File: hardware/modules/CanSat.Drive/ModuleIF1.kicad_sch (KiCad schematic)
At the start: 12 parts, among them J5 Jumper, J6 Conn_01x04_MountingPin, U11 TCK106AF, U12 INA226

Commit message: シート追加
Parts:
- removed J5: Jumper, Connector_PinHeader_1.27mm:PinHeader_1x02_P1.27mm_Vertical, symbol Connector:Conn_01x02_Pin
- removed R23: 10k, Resistor_SMD:R_0402_1005Metric, symbol Device:R
- removed R26: 120, Resistor_SMD:R_0402_1005Metric, symbol Device:R
- removed U11: TCK106AF, WOBCLibrary:WCSPD-4(0.8x0.8), symbol WOBCLibrary:TCK106AF
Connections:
- net VIN renamed VOUT
- no-connect marks 0 -> 1

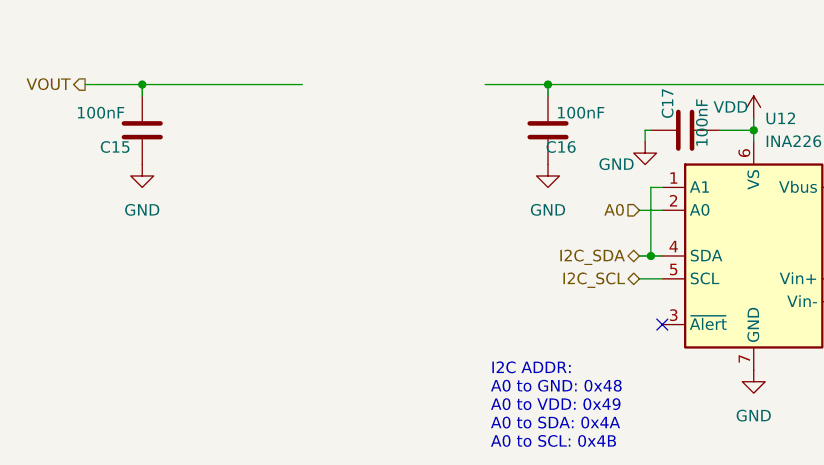
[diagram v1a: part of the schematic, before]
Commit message: 基板のフットプリントを作ったら回路図終わり
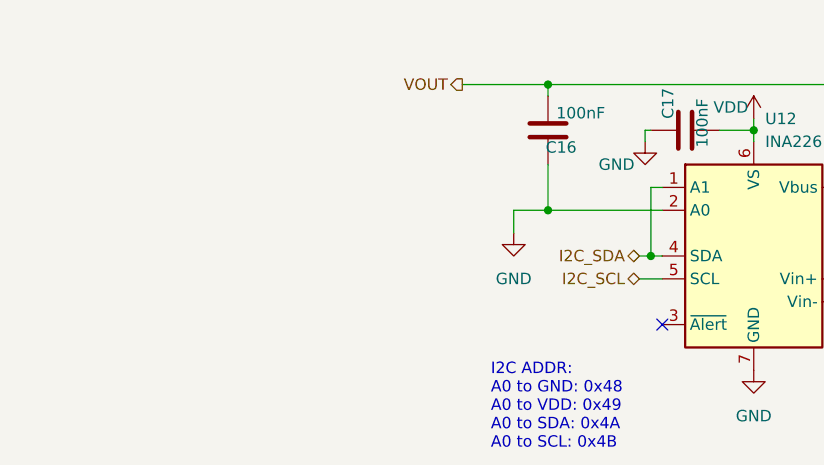
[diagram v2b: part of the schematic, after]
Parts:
- removed C15: 100nF, Capacitor_SMD:C_0402_1005Metric, symbol Device:C
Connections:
- net A0 is gone; now on net GND: U12.2 (A0)
- net VOUT: now also C16.2, R24.1, U12.10 (Vin+), U12.8 (Vbus)
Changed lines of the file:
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@@
 	)
 	(junction
-		(at 50.8 68.58)
+		(at 95.885 82.55)
 		(diameter 0)
 		(color 0 0 0 0)
@@
 	(wire
 		(pts
-			(xy 106.045 82.55) (xy 108.585 82.55)
+			(xy 95.885 82.55) (xy 108.585 82.55)
 		)
 		(stroke
@@
 	(wire
 		(pts
+			(xy 92.075 82.55) (xy 95.885 82.55)
+		)
+		(stroke
+			(width 0)
+			(type default)
+		)
+	)
+	(wire
+		(pts
 			(xy 107.315 80.01) (xy 107.315 87.63)
 		)
@@
 	(wire
 		(pts
-			(xy 44.45 68.58) (xy 50.8 68.58)
-		)
-		(stroke
-			(width 0)
-			(type default)
-		)
-	)
-	(wire
-		(pts
 			(xy 151.13 68.58) (xy 151.13 71.755)
 		)
@@
 	(wire
 		(pts
+			(xy 95.885 82.55) (xy 95.885 77.47)
+		)
+		(stroke
+			(width 0)
+			(type default)
+		)
+	)
+	(wire
+		(pts
 			(xy 106.045 87.63) (xy 107.315 87.63)
 		)
@@
 	(wire
 		(pts
-			(xy 50.8 68.58) (xy 50.8 69.85)
-		)
-		(stroke
-			(width 0)
-			(type default)
-		)
-	)
-	(wire
-		(pts
 			(xy 95.885 68.58) (xy 130.81 68.58)
 		)
@@
 	(wire
 		(pts
-			(xy 50.8 68.58) (xy 68.58 68.58)
+			(xy 86.36 68.58) (xy 95.885 68.58)
 		)
 		(stroke
@@
 	(wire
 		(pts
-			(xy 88.9 68.58) (xy 95.885 68.58)
-		)
-		(stroke
-			(width 0)
-			(type default)
-		)
-	)
-	(wire
-		(pts
 			(xy 130.81 68.58) (xy 130.81 80.01)
 		)
@@
 		(pts
 			(xy 118.745 73.66) (xy 118.745 74.93)
+		)
+		(stroke
+			(width 0)
+			(type default)
+		)
+	)
+	(wire
+		(pts
+			(xy 92.075 82.55) (xy 92.075 85.09)
 		)
 		(stroke
@@
 		)
 	)
-	(hierarchical_label "A0"
-		(shape input)
-		(at 106.045 82.55 180)
-		(fields_autoplaced yes)
-		(effects
-			(font
-				(size 1.27 1.27)
-			)
-			(justify right)
-		)
-	)
 	(hierarchical_label "I2C_SCL"
 		(shape bidirectional)
@@
 	(hierarchical_label "VOUT"
 		(shape output)
-		(at 44.45 68.58 180)
+		(at 86.36 68.58 180)
 		(fields_autoplaced yes)
 		(effects
@@
 			(project "GS"
 				(path "/953562b0-9f42-4c3d-8516-f6de553e7f3f/7e3ff05b-2209-4e68-8cf1-b7b284998fcd"
-					(reference "LED6")
+					(reference "LED301")
 					(unit 1)
 				)
@@
 			(project "GS"
 				(path "/953562b0-9f42-4c3d-8516-f6de553e7f3f/7e3ff05b-2209-4e68-8cf1-b7b284998fcd"
-					(reference "J6")
+					(reference "J301")
 					(unit 1)
 				)
@@
 			(project "GS"
 				(path "/953562b0-9f42-4c3d-8516-f6de553e7f3f/7e3ff05b-2209-4e68-8cf1-b7b284998fcd"
-					(reference "#PWR060")
+					(reference "#PWR0306")
 					(unit 1)
 				)
@@
 			(project "GS"
 				(path "/953562b0-9f42-4c3d-8516-f6de553e7f3f/7e3ff05b-2209-4e68-8cf1-b7b284998fcd"
-					(reference "U12")
+					(reference "U301")
 					(unit 1)
 				)
@@
 			(project "GS"
 				(path "/953562b0-9f42-4c3d-8516-f6de553e7f3f/7e3ff05b-2209-4e68-8cf1-b7b284998fcd"
-					(reference "#PWR059")
+					(reference "#PWR0305")
 					(unit 1)
 				)
@@
 			(project "GS"
 				(path "/953562b0-9f42-4c3d-8516-f6de553e7f3f/7e3ff05b-2209-4e68-8cf1-b7b284998fcd"
-					(reference "R25")
+					(reference "R302")
 					(unit 1)
 				)
@@
 			(project "GS"
 				(path "/953562b0-9f42-4c3d-8516-f6de553e7f3f/7e3ff05b-2209-4e68-8cf1-b7b284998fcd"
-					(reference "C17")
+					(reference "C302")
 					(unit 1)
 				)
@@
 			(project "GS"
 				(path "/953562b0-9f42-4c3d-8516-f6de553e7f3f/7e3ff05b-2209-4e68-8cf1-b7b284998fcd"
-					(reference "#PWR056")
+					(reference "#PWR0302")
 					(unit 1)
 				)
@@
 			(project "GS"
 				(path "/953562b0-9f42-4c3d-8516-f6de553e7f3f/7e3ff05b-2209-4e68-8cf1-b7b284998fcd"
-					(reference "#PWR058")
+					(reference "#PWR0304")
 					(unit 1)
 				)
@@
 				(path "/d339b9d8-51a7-460e-bb19-8d8c25d3e2aa"
 					(reference "#PWR0106")
-					(unit 1)
-				)
-			)
-		)
-	)
-	(symbol
-		(lib_id "power:GND")
-		(at 50.8 77.47 0)
-		(unit 1)
-		(exclude_from_sim no)
-		(in_bom yes)
-		(on_board yes)
-		(dnp no)
-		(fields_autoplaced yes)
-		(property "Reference" "#PWR053"
-			(at 50.8 83.82 0)
-			(effects
-				(font
-					(size 1.27 1.27)
-				)
-				(hide yes)
-			)
-		)
-		(property "Value" "GND"
-			(at 50.8 82.55 0)
-			(effects
-				(font
-					(size 1.27 1.27)
-				)
-			)
-		)
-		(property "Footprint" ""
-			(at 50.8 77.47 0)
-			(effects
-				(font
-					(size 1.27 1.27)
-				)
-				(hide yes)
-			)
-		)
-		(property "Datasheet" ""
-			(at 50.8 77.47 0)
-			(effects
-				(font
-					(size 1.27 1.27)
-				)
-				(hide yes)
-			)
-		)
-		(property "Description" ""
-			(at 50.8 77.47 0)
-			(effects
-				(font
-					(size 1.27 1.27)
-				)
-				(hide yes)
-			)
-		)
-		(pin "1"
-		)
-		(instances
-			(project "GS"
-				(path "/920f9ee9-d8de-4f24-ad72-1c45434a67fe/deff5b4c-9f0c-4d0a-bd9e-e7e67942e2ab"
-					(reference "#PWR053")
-					(unit 1)
-				)
-			)
-			(project "GS"
-				(path "/953562b0-9f42-4c3d-8516-f6de553e7f3f/7e3ff05b-2209-4e68-8cf1-b7b284998fcd"
-					(reference "#PWR053")
-					(unit 1)
-				)
-			)
-			(project "ModuleIF"
-				(path "/d339b9d8-51a7-460e-bb19-8d8c25d3e2aa"
-					(reference "#PWR0101")
 					(unit 1)
 				)
@@
 			(project "GS"
 				(path "/953562b0-9f42-4c3d-8516-f6de553e7f3f/7e3ff05b-2209-4e68-8cf1-b7b284998fcd"
-					(reference "R24")
+					(reference "R301")
 					(unit 1)
 				)
@@
 			(project "GS"
 				(path "/953562b0-9f42-4c3d-8516-f6de553e7f3f/7e3ff05b-2209-4e68-8cf1-b7b284998fcd"
-					(reference "#PWR061")
+					(reference "#PWR0307")
 					(unit 1)
 				)
@@
 	(symbol
 		(lib_id "power:GND")
-		(at 95.885 77.47 0)
+		(at 92.075 85.09 0)
 		(unit 1)
 		(exclude_from_sim no)
@@
 		(fields_autoplaced yes)
 		(property "Reference" "#PWR055"
-			(at 95.885 83.82 0)
+			(at 92.075 91.44 0)
 			(effects
 				(font
@@
 		)
 		(property "Value" "GND"
-			(at 95.885 82.55 0)
+			(at 92.075 90.17 0)
 			(effects
 				(font
@@
 		)
 		(property "Footprint" ""
-			(at 95.885 77.47 0)
+			(at 92.075 85.09 0)
 			(effects
 				(font
@@
 		)
 		(property "Datasheet" ""
-			(at 95.885 77.47 0)
+			(at 92.075 85.09 0)
 			(effects
 				(font
@@
 		)
 		(property "Description" ""
-			(at 95.885 77.47 0)
+			(at 92.075 85.09 0)
 			(effects
 				(font
@@
 			(project "GS"
 				(path "/953562b0-9f42-4c3d-8516-f6de553e7f3f/7e3ff05b-2209-4e68-8cf1-b7b284998fcd"
-					(reference "#PWR055")
+					(reference "#PWR0301")
 					(unit 1)
 				)
@@
 				(path "/d339b9d8-51a7-460e-bb19-8d8c25d3e2aa"
 					(reference "#PWR0103")
-					(unit 1)
-				)
-			)
-		)
-	)
-	(symbol
-		(lib_id "Device:C")
-		(at 50.8 73.66 180)
-		(unit 1)
-		(exclude_from_sim no)
-		(in_bom yes)
-		(on_board yes)
-		(dnp no)
-		(property "Reference" "C15"
-			(at 49.53 75.565 0)
-			(effects
-				(font
-					(size 1.27 1.27)
-				)
-				(justify left)
-			)
-		)
-		(property "Value" "100nF"
-			(at 48.895 71.755 0)
-			(effects
-				(font
-					(size 1.27 1.27)
-				)
-				(justify left)
-			)
-		)
-		(property "Footprint" "Capacitor_SMD:C_0402_1005Metric"
-			(at 49.8348 69.85 0)
-			(effects
-				(font
-					(size 1.27 1.27)
-				)
-				(hide yes)
-			)
-		)
-		(property "Datasheet" "~"
-			(at 50.8 73.66 0)
-			(effects
-				(font
-					(size 1.27 1.27)
-				)
-				(hide yes)
-			)
-		)
-		(property "Description" ""
-			(at 50.8 73.66 0)
-			(effects
-				(font
-					(size 1.27 1.27)
-				)
-				(hide yes)
-			)
-		)
-		(property "LCSC" "C1525"
-			(at 50.8 73.66 0)
-			(effects
-				(font
-					(size 1.27 1.27)
-				)
-				(hide yes)
-			)
-		)
-		(pin "1"
-		)
-		(pin "2"
-		)
-		(instances
-			(project "GS"
-				(path "/920f9ee9-d8de-4f24-ad72-1c45434a67fe/deff5b4c-9f0c-4d0a-bd9e-e7e67942e2ab"
-					(reference "C15")
-					(unit 1)
-				)
-			)
-			(project "GS"
-				(path "/953562b0-9f42-4c3d-8516-f6de553e7f3f/7e3ff05b-2209-4e68-8cf1-b7b284998fcd"
-					(reference "C15")
-					(unit 1)
-				)
-			)
-			(project "ModuleIF"
-				(path "/d339b9d8-51a7-460e-bb19-8d8c25d3e2aa"
-					(reference "C101")
-					(unit 1)
-				)
-			)
-			(project "LiPoPowerSimple"
-				(path "/ed97c6c4-a1a7-4dde-a640-89eca815dd0d"
-					(reference "C9")
 					(unit 1)
 				)
@@
 			(project "GS"
 				(path "/953562b0-9f42-4c3d-8516-f6de553e7f3f/7e3ff05b-2209-4e68-8cf1-b7b284998fcd"
-					(reference "#PWR057")
+					(reference "#PWR0303")
 					(unit 1)
 				)
@@
 			(project "GS"
 				(path "/953562b0-9f42-4c3d-8516-f6de553e7f3f/7e3ff05b-2209-4e68-8cf1-b7b284998fcd"
-					(reference "C16")
-					(unit 1)
-				)
+					(reference "C301")
+					(unit 1)
+				)

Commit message: 配置完了
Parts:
- removed C16, C17: 100nF, Capacitor_SMD:C_0402_1005Metric, symbol Device:C
- removed R24: 50mΩ, Resistor_SMD:R_0805_2012Metric, symbol Device:R
- removed U12: INA226, Package_SO:VSSOP-10_3x3mm_P0.5mm, symbol Sensor_Energy:INA226
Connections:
- net VOUT: now also J6.3 (Pin_3), R25.2
- no-connect marks 1 -> 0
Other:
- note removed: "I2C ADDR: A0 to GND: 0x48 A0 to VDD: 0x49 A0 to SDA: 0x4A A0 to SCL: 0x4B"
